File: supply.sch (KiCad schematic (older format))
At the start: 44 parts, among them IC1 MIC5317-2.5YM5-TR, J1 WE_629105150521, U1 FT2232HL-REEL, U2 NCP163ASN330T1G, Y1 KX-7_12,MHz

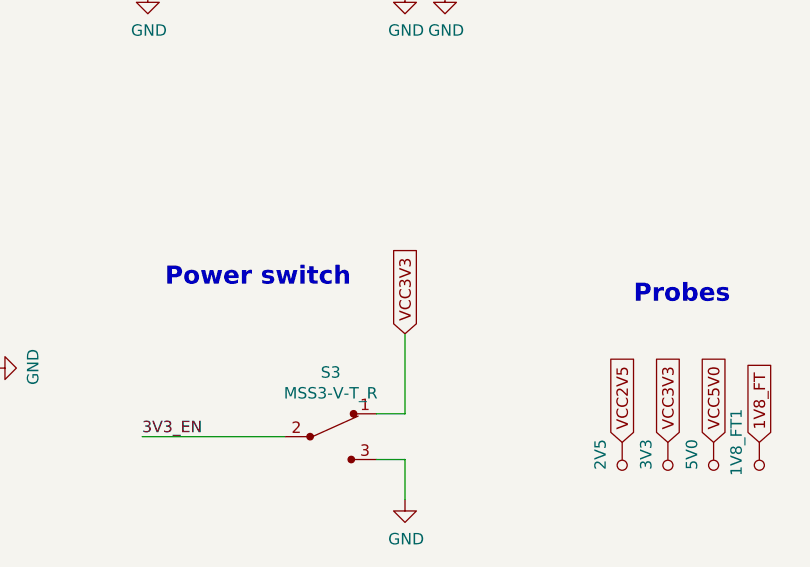
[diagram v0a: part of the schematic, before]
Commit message: Fix 3V3 EN signal - bump rev. to 1.0.2
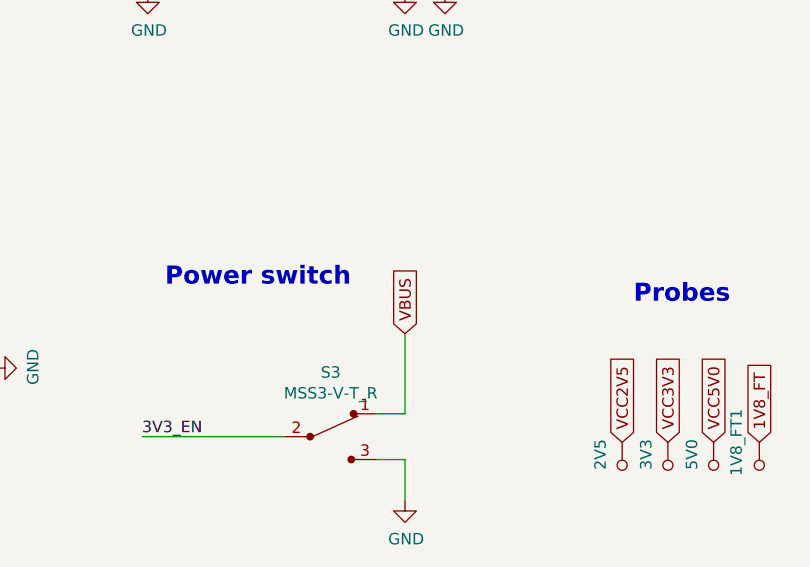
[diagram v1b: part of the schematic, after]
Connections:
- net VBUS: now also S3.1
- net VCC3V3: no longer S3.1
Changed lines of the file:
@@
 Title "RDIMM-breakout"
 Date "2021-10"
-Rev "1.0.1"
+Rev "1.0.2"
 Comp "Antmicro Ltd."
 Comment1 "www.antmicro.com"
@@
 Wire Wire Line
 	3600 10425 3600 10075
-Text GLabel 3600 10075 1    50   Input ~ 0
-VCC3V3
 Wire Wire Line
 	3475 10425 3600 10425
@@
 	1    0    0    -1
 $EndComp
+Text GLabel 3600 10075 1    50   Input ~ 0
+VBUS
 $EndSCHEMATC

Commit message: Update naming convention
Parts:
- 1V8_FT1, 2V5, 3V3, 5V0: footprint rdimm-breakout-footprints:Testpoint_smd_1mm -> ddr4-spd-breakout-footprints:Testpoint_smd_1mm; symbol rdimm-breakout:TP_SMD1MM-rdimm-breakout -> ddr4-spd-breakout:TP_SMD1MM-ddr4-spd-breakout
- C1, C2, C3, C4: footprint rdimm-breakout-footprints:0402-cap -> ddr4-spd-breakout-footprints:0402-cap; symbol rdimm-breakout:C_1u_0402 -> ddr4-spd-breakout:C_1u_0402
- C10, C11, C13, C14, C15, C16, C19, C20, C21, C5, C8, C9: footprint rdimm-breakout-footprints:0402-cap -> ddr4-spd-breakout-footprints:0402-cap; symbol rdimm-breakout:C_100n_0402 -> ddr4-spd-breakout:C_100n_0402
- C12, C17, C18: footprint rdimm-breakout-footprints:0402-cap -> ddr4-spd-breakout-footprints:0402-cap; symbol rdimm-breakout:C_4u7_0402 -> ddr4-spd-breakout:C_4u7_0402
- C6, C7: footprint rdimm-breakout-footprints:0402-cap -> ddr4-spd-breakout-footprints:0402-cap; symbol rdimm-breakout:C_27p_0402 -> ddr4-spd-breakout:C_27p_0402
- D1: footprint rdimm-breakout-footprints:TPD2E009DRTR -> ddr4-spd-breakout-footprints:TPD2E009DRTR; symbol rdimm-breakout:PESD5V0S2BQA -> ddr4-spd-breakout:PESD5V0S2BQA
- FB1, FB2, FB3: footprint rdimm-breakout-footprints:0603 -> ddr4-spd-breakout-footprints:0603; symbol rdimm-breakout:BLM18AG601SN1D -> ddr4-spd-breakout:BLM18AG601SN1D
- IC1: footprint rdimm-breakout-footprints:SOT-23-5 -> ddr4-spd-breakout-footprints:SOT-23-5; symbol rdimm-breakout:TPS7A0518PDBVT -> ddr4-spd-breakout:TPS7A0518PDBVT
- J1: footprint rdimm-breakout-footprints:USB_Micro_B_Female_629105150521 -> ddr4-spd-breakout-footprints:USB_Micro_B_Female_629105150521; symbol rdimm-breakout:WE_629105150521 -> ddr4-spd-breakout:WE_629105150521
- PWR1: footprint rdimm-breakout-footprints:LED_0603 -> ddr4-spd-breakout-footprints:LED_0603; symbol rdimm-breakout:KP-1608CGCK-rdimm-breakout -> ddr4-spd-breakout:KP-1608CGCK-ddr4-spd-breakout
- R1, R5, R6: footprint rdimm-breakout-footprints:0603-res -> ddr4-spd-breakout-footprints:0603-res; symbol rdimm-breakout:R_0R_0603 -> ddr4-spd-breakout:R_0R_0603
- R119: footprint rdimm-breakout-footprints:0402-res -> ddr4-spd-breakout-footprints:0402-res; symbol rdimm-breakout:R_330R_0402-rdimm-breakout -> ddr4-spd-breakout:R_330R_0402-ddr4-spd-breakout
- R2: footprint rdimm-breakout-footprints:0402-res -> ddr4-spd-breakout-footprints:0402-res; symbol rdimm-breakout:R_4k7_0402 -> ddr4-spd-breakout:R_4k7_0402
- R3: footprint rdimm-breakout-footprints:0402-res -> ddr4-spd-breakout-footprints:0402-res; symbol rdimm-breakout:R_10k_0402 -> ddr4-spd-breakout:R_10k_0402
- R4: footprint rdimm-breakout-footprints:0402-res -> ddr4-spd-breakout-footprints:0402-res; symbol rdimm-breakout:R_12k_0402 -> ddr4-spd-breakout:R_12k_0402
- R7: footprint rdimm-breakout-footprints:0402-res -> ddr4-spd-breakout-footprints:0402-res; symbol rdimm-breakout:R_220R_0402 -> ddr4-spd-breakout:R_220R_0402
- S3: footprint rdimm-breakout-footprints:Switch_Slide_MSS3 -> ddr4-spd-breakout-footprints:Switch_Slide_MSS3; symbol rdimm-breakout:MSS3-V-T_R -> ddr4-spd-breakout:MSS3-V-T_R
- U1: footprint rdimm-breakout-footprints:LQFP-64_10x10mm -> ddr4-spd-breakout-footprints:LQFP-64_10x10mm; symbol rdimm-breakout:FT2232HL-REEL -> ddr4-spd-breakout:FT2232HL-REEL
- U2: footprint rdimm-breakout-footprints:SOT-23-5 -> ddr4-spd-breakout-footprints:SOT-23-5; symbol rdimm-breakout:NCP163ASN330T1G -> ddr4-spd-breakout:NCP163ASN330T1G
- Y1: footprint rdimm-breakout-footprints:KX-7 -> ddr4-spd-breakout-footprints:KX-7; symbol rdimm-breakout:KX-7_12,MHz -> ddr4-spd-breakout:KX-7_12,MHz
